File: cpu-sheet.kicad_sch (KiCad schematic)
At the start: 54 parts, among them J3 GPIO_HEADER, J4 GPIOR_HEADER, J5 USB_B_Micro, J6 PROG_CONN, U11 CH340G, U6 SRV05-4, U7 23LC1024, U8 STM32L432KC, U9 SRV05-4, Y2 32.768K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

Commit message: leds to be 0805, also TX (red) -- silk adjustments
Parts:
- D17, D18, D6: footprint LED_SMD:LED_0603_1608Metric -> LED_SMD:LED_0805_2012Metric; LCSC C72043 -> C2297
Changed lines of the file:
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@@
 			)
 		)
-		(property "Footprint" "LED_SMD:LED_0603_1608Metric"
+		(property "Footprint" "LED_SMD:LED_0805_2012Metric"
 			(at 63.5 144.78 0)
 			(effects
@@
 			)
 		)
-		(property "LCSC" "C72043"
+		(property "LCSC" "C2297"
 			(at 63.5 144.78 0)
 			(effects
@@
 			)
 		)
-		(property "Footprint" "LED_SMD:LED_0603_1608Metric"
+		(property "Footprint" "LED_SMD:LED_0805_2012Metric"
 			(at 203.2 73.66 0)
 			(effects
@@
 			)
 		)
-		(property "LCSC" "C72043"
+		(property "LCSC" "C2297"
 			(at 203.2 73.66 0)
 			(effects
@@
 			)
 		)
-		(property "Footprint" "LED_SMD:LED_0603_1608Metric"
+		(property "Footprint" "LED_SMD:LED_0805_2012Metric"
 			(at 254 73.66 0)
 			(effects
@@
 			)
 		)
-		(property "LCSC" "C72043"
+		(property "LCSC" "C2297"
 			(at 254 73.66 0)
 			(effects

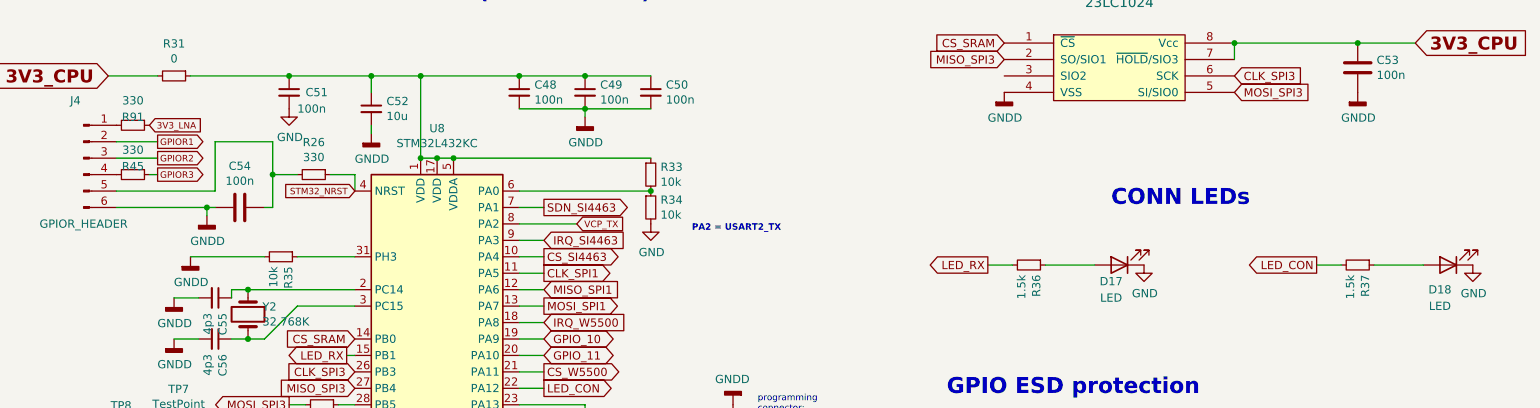
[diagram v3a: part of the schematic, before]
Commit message: add resistor R93 to make RX_STATE to be RX_LED on header J4
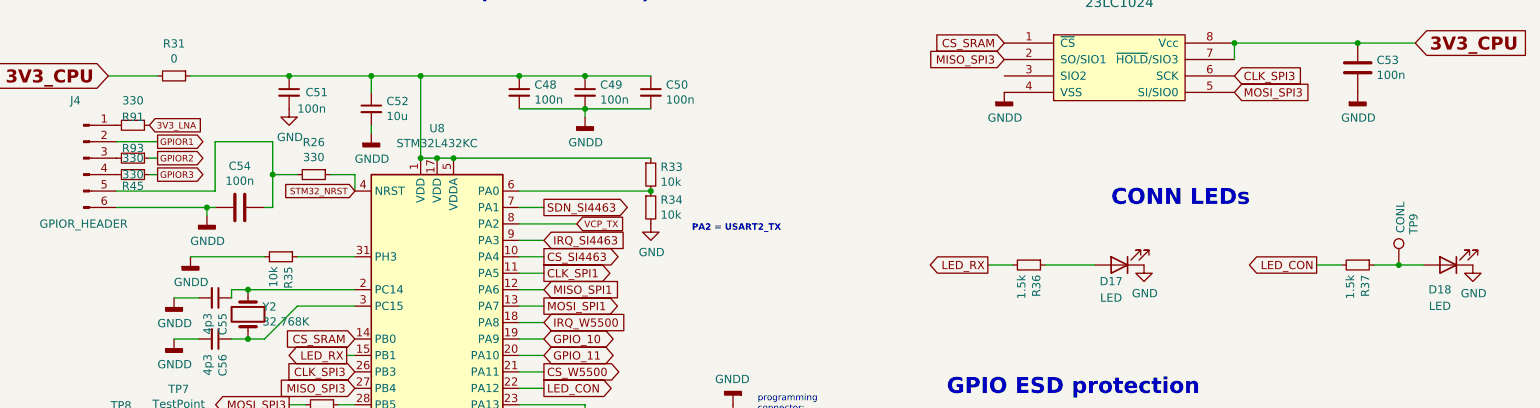
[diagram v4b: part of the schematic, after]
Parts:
- added R93: 330, Resistor_SMD:R_0603_1608Metric, symbol Device:R_Small
- added TP9: CONL, TestPoint:TestPoint_Pad_D1.5mm, symbol Connector:TestPoint
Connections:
- net GPIOR2: now also R93.1; no longer J4.3 (Pin_3)
- net at D18.2 (A), R37.1: now also TP9.1
- new net: J4.3 (Pin_3), R93.2
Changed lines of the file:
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@@
 	)
 	(junction
+		(at 246.38 73.66)
+		(diameter 0)
+		(color 0 0 0 0)
+	)
+	(junction
 		(at 130.81 62.23)
 		(diameter 0)
@@
 	(wire
 		(pts
-			(xy 48.26 57.15) (xy 54.61 57.15)
-		)
-		(stroke
-			(width 0)
-			(type default)
-		)
-	)
-	(wire
-		(pts
 			(xy 110.49 90.17) (xy 114.3 90.17)
 		)
@@
 	(wire
 		(pts
+			(xy 246.38 73.66) (xy 250.19 73.66)
+		)
+		(stroke
+			(width 0)
+			(type default)
+		)
+	)
+	(wire
+		(pts
 			(xy 204.47 111.76) (xy 204.47 105.41)
 		)
@@
 	(wire
 		(pts
-			(xy 242.57 73.66) (xy 250.19 73.66)
+			(xy 242.57 73.66) (xy 246.38 73.66)
 		)
 		(stroke
@@
 	(wire
 		(pts
+			(xy 53.34 57.15) (xy 54.61 57.15)
+		)
+		(stroke
+			(width 0)
+			(type default)
+		)
+	)
+	(wire
+		(pts
 			(xy 110.49 82.55) (xy 114.3 82.55)
 		)
@@
 		(dnp no)
 		(property "Reference" "R45"
-			(at 50.8 58.42 90)
+			(at 50.8 61.468 90)
 			(effects
 				(font
@@
 		)
 		(property "Value" "330"
-			(at 50.8 55.88 90)
+			(at 50.8 59.69 90)
 			(effects
 				(font
@@
 					(unit 1)
 				)
+			)
+		)
+	)
+	(symbol
+		(lib_id "Connector:TestPoint")
+		(at 246.38 73.66 0)
+		(unit 1)
+		(exclude_from_sim no)
+		(in_bom yes)
+		(on_board yes)
+		(dnp no)
+		(property "Reference" "TP9"
+			(at 248.666 67.31 90)
+			(effects
+				(font
+					(size 1.27 1.27)
+				)
+			)
+		)
+		(property "Value" "CONL"
+			(at 246.634 66.294 90)
+			(effects
+				(font
+					(size 1.27 1.27)
+				)
+			)
+		)
+		(property "Footprint" "TestPoint:TestPoint_Pad_D1.5mm"
+			(at 251.46 73.66 0)
+			(effects
+				(font
+					(size 1.27 1.27)
+				)
+				(hide yes)
+			)
+		)
+		(property "Datasheet" "~"
+			(at 251.46 73.66 0)
+			(effects
+				(font
+					(size 1.27 1.27)
+				)
+				(hide yes)
+			)
+		)
+		(property "Description" ""
+			(at 246.38 73.66 0)
+			(effects
+				(font
+					(size 1.27 1.27)
+				)
+				(hide yes)
+			)
+		)
+		(property "DNP" "TRUE"
+			(at 246.38 73.66 0)
+			(effects
+				(font
+					(size 1.27 1.27)
+				)
+				(hide yes)
+			)
+		)
+		(pin "1"
+		)
+		(instances
+			(project "TACNPR"
+				(path "/9538e4ed-27e6-4c37-b989-9859dc0d49e8/00000000-0000-0000-0000-00006096f497"
+					(reference "TP9")
+					(unit 1)
+				)
+			)
+		)
+	)
+	(symbol
+		(lib_id "Device:R_Small")
+		(at 50.8 57.15 270)
+		(unit 1)
+		(exclude_from_sim no)
+		(in_bom yes)
+		(on_board yes)
+		(dnp no)
+		(property "Reference" "R93"
+			(at 50.8 55.626 90)
+			(effects
+				(font
+					(size 1.27 1.27)
+				)
+			)
+		)
+		(property "Value" "330"
+			(at 50.8 57.15 90)
+			(effects
+				(font
+					(size 1.27 1.27)
+				)
+			)
+		)
+		(property "Footprint" "Resistor_SMD:R_0603_1608Metric"
+			(at 50.8 57.15 0)
+			(effects
+				(font
+					(size 1.27 1.27)
+				)
+				(hide yes)
+			)
+		)
+		(property "Datasheet" "~"
+			(at 50.8 57.15 0)
+			(effects
+				(font
+					(size 1.27 1.27)
+				)
+				(hide yes)
+			)
+		)
+		(property "Description" ""
+			(at 50.8 57.15 0)
+			(effects
+				(font
+					(size 1.27 1.27)
+				)
+				(hide yes)
+			)
+		)
+		(property "LCSC" "C23138"
+			(at 50.8 57.15 0)
+			(effects
+				(font
+					(size 1.27 1.27)
+				)
+				(hide yes)
+			)
+		)
+		(pin "1"
+		)
+		(pin "2"
+		)
+		(instances
+			(project "TACNPR"
+				(path "/9538e4ed-27e6-4c37-b989-9859dc0d49e8/00000000-0000-0000-0000-00006096f497"
+					(reference "R93")
+					(unit 1)
+				)

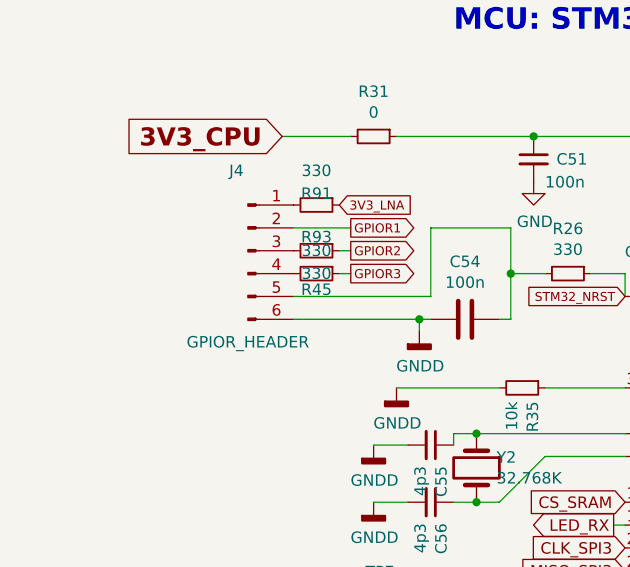
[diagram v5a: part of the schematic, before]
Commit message: replace RX STATE LED by RXLED on header J4, R45 added
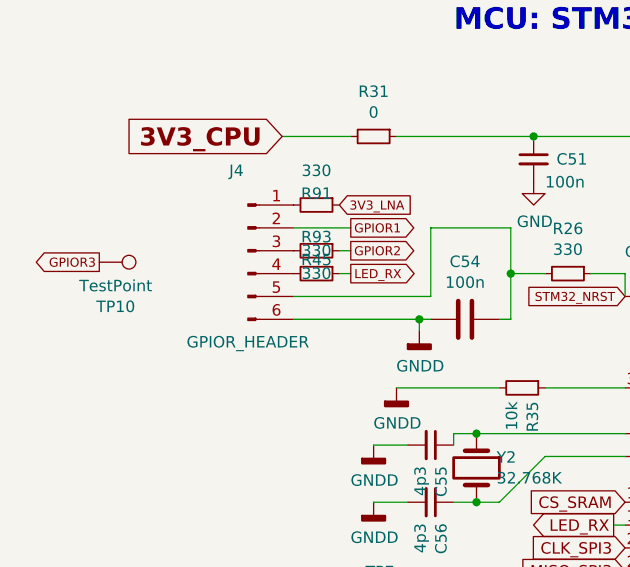
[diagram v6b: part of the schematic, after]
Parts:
- added TP10: TestPoint, TestPoint:TestPoint_Pad_D1.5mm, symbol Connector:TestPoint
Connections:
- net GPIOR3: now also TP10.1; no longer R45.1
- net LED_RX: now also R45.1
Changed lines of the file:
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@@
 	(wire
 		(pts
-			(xy 53.34 59.69) (xy 54.61 59.69)
-		)
-		(stroke
-			(width 0)
-			(type default)
-		)
-	)
-	(wire
-		(pts
 			(xy 43.18 156.21) (xy 43.18 161.29)
 		)
@@
 	(wire
 		(pts
+			(xy 54.61 59.69) (xy 53.34 59.69)
+		)
+		(stroke
+			(width 0)
+			(type default)
+		)
+	)
+	(wire
+		(pts
 			(xy 191.77 73.66) (xy 199.39 73.66)
 		)
@@
 		)
 	)
+	(global_label "GPIOR3"
+		(shape output)
+		(at 26.67 58.42 180)
+		(fields_autoplaced yes)
+		(effects
+			(font
+				(size 1.0038 1.0038)
+			)
+			(justify right)
+		)
+		(property "Intersheetrefs" "${INTERSHEET_REFS}"
+			(at 19.3305 58.42 0)
+			(effects
+				(font
+					(size 1.0038 1.0038)
+				)
+				(justify right)
+				(hide yes)
+			)
+		)
+	)
 	(global_label "CS_SRAM"
 		(shape input)
@@
 		)
 	)
+	(global_label "LED_RX"
+		(shape output)
+		(at 54.61 59.69 0)
+		(fields_autoplaced yes)
+		(effects
+			(font
+				(size 1 1)
+			)
+			(justify left)
+		)
+		(property "Intersheetrefs" "${INTERSHEET_REFS}"
+			(at 61.8739 59.69 0)
+			(effects
+				(font
+					(size 1.27 1.27)
+				)
+				(justify left)
+				(hide yes)
+			)
+		)
+	)
 	(global_label "CLK_SPI3"
 		(shape input)
@@
 		)
 	)
-	(global_label "GPIOR3"
-		(shape output)
-		(at 54.61 59.69 0)
-		(fields_autoplaced yes)
-		(effects
-			(font
-				(size 1.0038 1.0038)
-			)
-			(justify left)
-		)
-		(property "Intersheetrefs" "${INTERSHEET_REFS}"
-			(at 61.944 59.6273 0)
-			(effects
-				(font
-					(size 1.0038 1.0038)
-				)
-				(justify left)
-				(hide yes)
-			)
-		)
-	)
 	(symbol
 		(lib_id "Device:C_Small")
@@
 	(symbol
 		(lib_id "Device:R_Small")
-		(at 50.8 59.69 270)
+		(at 50.8 52.07 270)
 		(unit 1)
 		(exclude_from_sim no)
@@
 		(on_board yes)
 		(dnp no)
-		(property "Reference" "R45"
-			(at 50.8 61.468 90)
+		(property "Reference" "R91"
+			(at 50.8 50.8 90)
 			(effects
 				(font
@@
 		)
 		(property "Value" "330"
-			(at 50.8 59.69 90)
+			(at 50.8 48.26 90)
 			(effects
 				(font
@@
 		)
 		(property "Footprint" "Resistor_SMD:R_0603_1608Metric"
-			(at 50.8 59.69 0)
+			(at 50.8 52.07 0)
 			(effects
 				(font
@@
 		)
 		(property "Datasheet" "~"
-			(at 50.8 59.69 0)
+			(at 50.8 52.07 0)
 			(effects
 				(font
@@
 		)
 		(property "Description" ""
-			(at 50.8 59.69 0)
+			(at 50.8 52.07 0)
 			(effects
 				(font
@@
 		)
 		(property "LCSC" "C23138"
-			(at 50.8 59.69 0)
+			(at 50.8 52.07 0)
 			(effects
 				(font
@@
 			(project "TACNPR"
 				(path "/9538e4ed-27e6-4c37-b989-9859dc0d49e8/00000000-0000-0000-0000-00006096f497"
-					(reference "R45")
+					(reference "R91")
 					(unit 1)
 				)
@@
 	)
 	(symbol
-		(lib_id "Device:R_Small")
-		(at 50.8 52.07 270)
+		(lib_id "Connector:Conn_01x06_Male")
+		(at 43.18 57.15 0)
 		(unit 1)
 		(exclude_from_sim no)
@@
 		(on_board yes)
 		(dnp no)
-		(property "Reference" "R91"
-			(at 50.8 50.8 90)
+		(property "Reference" "J4"
+			(at 41.91 48.26 0)
 			(effects
 				(font
@@
 			)
 		)
-		(property "Value" "330"
-			(at 50.8 48.26 90)
+		(property "Value" "GPIOR_HEADER"
+			(at 43.18 67.31 0)
 			(effects
 				(font
@@
 			)
 		)
-		(property "Footprint" "Resistor_SMD:R_0603_1608Metric"
-			(at 50.8 52.07 0)
+		(property "Footprint" "Connector_PinHeader_2.54mm:PinHeader_1x06_P2.54mm_Vertical_SMD_Pin1Left"
+			(at 43.18 57.15 0)
 			(effects
 				(font
@@
 		)
 		(property "Datasheet" "~"
-			(at 50.8 52.07 0)
+			(at 43.18 57.15 0)
 			(effects
 				(font
@@
 		)
 		(property "Description" ""
-			(at 50.8 52.07 0)
+			(at 43.18 57.15 0)
 			(effects
 				(font
@@
 			)
 		)
-		(property "LCSC" "C23138"
-			(at 50.8 52.07 0)
+		(property "LCSC" "C5160789"
+			(at 43.18 57.15 0)
 			(effects
 				(font
@@
 		(pin "2"
 		)
+		(pin "3"
+		)
+		(pin "4"
+		)
+		(pin "5"
+		)
+		(pin "6"
+		)
 		(instances
 			(project "TACNPR"
 				(path "/9538e4ed-27e6-4c37-b989-9859dc0d49e8/00000000-0000-0000-0000-00006096f497"
-					(reference "R91")
+					(reference "J4")
 					(unit 1)
 				)
@@
 	)
 	(symbol
-		(lib_id "Connector:Conn_01x06_Male")
-		(at 43.18 57.15 0)
+		(lib_id "Connector:TestPoint")
+		(at 26.67 58.42 270)
 		(unit 1)
 		(exclude_from_sim no)
@@
 		(on_board yes)
 		(dnp no)
-		(property "Reference" "J4"
-			(at 41.91 48.26 0)
+		(property "Reference" "TP10"
+			(at 28.4988 63.373 90)
 			(effects
 				(font
@@
 			)
 		)
-		(property "Value" "GPIOR_HEADER"
-			(at 43.18 67.31 0)
+		(property "Value" "TestPoint"
+			(at 28.4988 61.0616 90)
 			(effects
 				(font
@@
 			)
 		)
-		(property "Footprint" "Connector_PinHeader_2.54mm:PinHeader_1x06_P2.54mm_Vertical_SMD_Pin1Left"
-			(at 43.18 57.15 0)
+		(property "Footprint" "TestPoint:TestPoint_Pad_D1.5mm"
+			(at 26.67 63.5 0)
 			(effects
 				(font
@@
 		)
 		(property "Datasheet" "~"
-			(at 43.18 57.15 0)
+			(at 26.67 63.5 0)
 			(effects
 				(font
@@
 		)
 		(property "Description" ""
-			(at 43.18 57.15 0)
+			(at 26.67 58.42 0)
 			(effects
 				(font
@@
 			)
 		)
-		(property "LCSC" "C5160789"
-			(at 43.18 57.15 0)
+		(property "DNP" "TRUE"
+			(at 26.67 58.42 0)
 			(effects
 				(font
@@
 		(pin "1"
 		)
-		(pin "2"
-		)
-		(pin "3"
-		)
-		(pin "4"
-		)
-		(pin "5"
-		)
-		(pin "6"
-		)
 		(instances
 			(project "TACNPR"
 				(path "/9538e4ed-27e6-4c37-b989-9859dc0d49e8/00000000-0000-0000-0000-00006096f497"
-					(reference "J4")
+					(reference "TP10")
 					(unit 1)
 				)
@@
 					(unit 1)
 				)
+			)
+		)
+	)
+	(symbol
+		(lib_id "Device:R_Small")
+		(at 50.8 59.69 270)
+		(unit 1)
+		(exclude_from_sim no)
+		(in_bom yes)
+		(on_board yes)
+		(dnp no)
+		(property "Reference" "R45"
+			(at 50.8 58.166 90)
+			(effects
+				(font
+					(size 1.27 1.27)
+				)
+			)
+		)
+		(property "Value" "330"
+			(at 50.8 59.69 90)
+			(effects
+				(font
+					(size 1.27 1.27)
+				)
+			)
+		)
+		(property "Footprint" "Resistor_SMD:R_0603_1608Metric"
+			(at 50.8 59.69 0)
+			(effects
+				(font
+					(size 1.27 1.27)
+				)
+				(hide yes)
+			)
+		)
+		(property "Datasheet" "~"
+			(at 50.8 59.69 0)
+			(effects
+				(font
+					(size 1.27 1.27)
+				)
+				(hide yes)
+			)
+		)
+		(property "Description" ""
+			(at 50.8 59.69 0)
+			(effects
+				(font
+					(size 1.27 1.27)
+				)
+				(hide yes)
+			)
+		)
+		(property "LCSC" "C23138"
+			(at 50.8 59.69 0)
+			(effects
+				(font
+					(size 1.27 1.27)
+				)
+				(hide yes)
+			)
+		)
+		(pin "1"
+		)
+		(pin "2"
+		)
+		(instances
+			(project "TACNPR"
+				(path "/9538e4ed-27e6-4c37-b989-9859dc0d49e8/00000000-0000-0000-0000-00006096f497"
+					(reference "R45")
+					(unit 1)
+				)

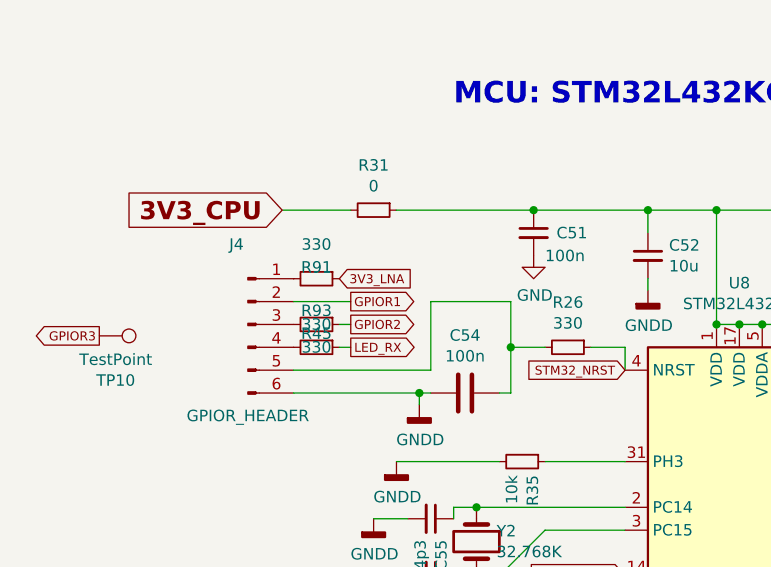
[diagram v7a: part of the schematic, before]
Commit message: J4 pin order correction
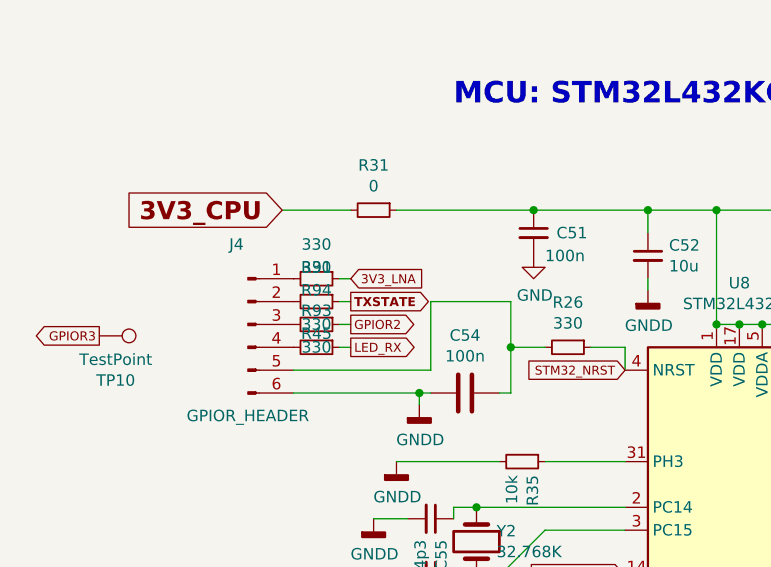
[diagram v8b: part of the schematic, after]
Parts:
- added R94: 330, Resistor_SMD:R_0603_1608Metric, symbol Device:R_Small
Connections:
- net GPIOR1: no longer names the net of J4.2 (Pin_2)
- net GPIOR1: now also R94.2
- new net TXSTATE: R94.1
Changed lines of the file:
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@@
 	(wire
 		(pts
+			(xy 53.34 54.61) (xy 54.61 54.61)
+		)
+		(stroke
+			(width 0)
+			(type default)
+		)
+	)
+	(wire
+		(pts
 			(xy 110.49 49.53) (xy 120.65 49.53)
 		)
@@
 	(wire
 		(pts
+			(xy 54.61 52.07) (xy 53.34 52.07)
+		)
+		(stroke
+			(width 0)
+			(type default)
+		)
+	)
+	(wire
+		(pts
 			(xy 114.3 85.09) (xy 110.49 85.09)
 		)
@@
 	(wire
 		(pts
-			(xy 48.26 54.61) (xy 54.61 54.61)
-		)
-		(stroke
-			(width 0)
-			(type default)
-		)
-	)
-	(wire
-		(pts
 			(xy 71.12 64.77) (xy 72.39 64.77)
 		)
@@
 		)
 	)
-	(global_label "LED_RX"
+	(global_label "TXSTATE"
 		(shape output)
-		(at 83.82 87.63 180)
+		(at 54.61 54.61 0)
 		(fields_autoplaced yes)
 		(effects
 			(font
-				(size 1.27 1.27)
+				(size 1 1)
+				(thickness 0.254)
+				(bold yes)
 			)
-			(justify right)
+			(justify left)
 		)
 		(property "Intersheetrefs" "${INTERSHEET_REFS}"
-			(at 0 0 0)
+			(at 63.0227 54.61 0)
 			(effects
 				(font
 					(size 1.27 1.27)
+					(thickness 0.254)
+					(bold yes)
 				)
+				(justify left)
 				(hide yes)
 			)
 		)
 	)
-	(global_label "CLK_SPI3"
-		(shape input)
-		(at 220.98 44.45 0)
+	(global_label "LED_RX"
+		(shape output)
+		(at 83.82 87.63 180)
 		(fields_autoplaced yes)
 		(effects
@@
 				(size 1.27 1.27)
 			)
-			(justify left)
+			(justify right)
 		)
 		(property "Intersheetrefs" "${INTERSHEET_REFS}"
@@
 		)
 	)
-	(global_label "GPIOR1"
-		(shape output)
-		(at 54.61 54.61 0)
+	(global_label "CLK_SPI3"
+		(shape input)
+		(at 220.98 44.45 0)
 		(fields_autoplaced yes)
 		(effects
 			(font
-				(size 1.0038 1.0038)
+				(size 1.27 1.27)
 			)
 			(justify left)
 		)
 		(property "Intersheetrefs" "${INTERSHEET_REFS}"
-			(at 61.944 54.5473 0)
+			(at 0 0 0)
 			(effects
 				(font
-					(size 1.0038 1.0038)
+					(size 1.27 1.27)
 				)
-				(justify left)
 				(hide yes)
 			)
@@
 	(global_label "3V3_LNA"
 		(shape input)
-		(at 53.34 52.07 0)
+		(at 54.61 52.07 0)
 		(fields_autoplaced yes)
 		(effects
@@
 		)
 		(property "Intersheetrefs" "${INTERSHEET_REFS}"
-			(at 61.4081 52.0075 0)
+			(at 62.6781 52.0075 0)
 			(effects
 				(font
@@
 					(unit 1)
 				)
+			)
+		)
+	)
+	(symbol
+		(lib_id "Device:R_Small")
+		(at 50.8 54.61 270)
+		(unit 1)
+		(exclude_from_sim no)
+		(in_bom yes)
+		(on_board yes)
+		(dnp no)
+		(property "Reference" "R94"
+			(at 50.8 53.34 90)
+			(effects
+				(font
+					(size 1.27 1.27)
+				)
+			)
+		)
+		(property "Value" "330"
+			(at 50.8 50.8 90)
+			(effects
+				(font
+					(size 1.27 1.27)
+				)
+			)
+		)
+		(property "Footprint" "Resistor_SMD:R_0603_1608Metric"
+			(at 50.8 54.61 0)
+			(effects
+				(font
+					(size 1.27 1.27)
+				)
+				(hide yes)
+			)
+		)
+		(property "Datasheet" "~"
+			(at 50.8 54.61 0)
+			(effects
+				(font
+					(size 1.27 1.27)
+				)
+				(hide yes)
+			)
+		)
+		(property "Description" ""
+			(at 50.8 54.61 0)
+			(effects
+				(font
+					(size 1.27 1.27)
+				)
+				(hide yes)
+			)
+		)
+		(property "LCSC" "C23138"
+			(at 50.8 54.61 0)
+			(effects
+				(font
+					(size 1.27 1.27)
+				)
+				(hide yes)
+			)
+		)
+		(pin "1"
+		)
+		(pin "2"
+		)
+		(instances
+			(project "TACNPR"
+				(path "/9538e4ed-27e6-4c37-b989-9859dc0d49e8/00000000-0000-0000-0000-00006096f497"
+					(reference "R94")
+					(unit 1)
+				)
